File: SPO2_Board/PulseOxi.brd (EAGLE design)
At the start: 70 x 70 mm, 45 parts, among them IC1 AFE4400RHAR

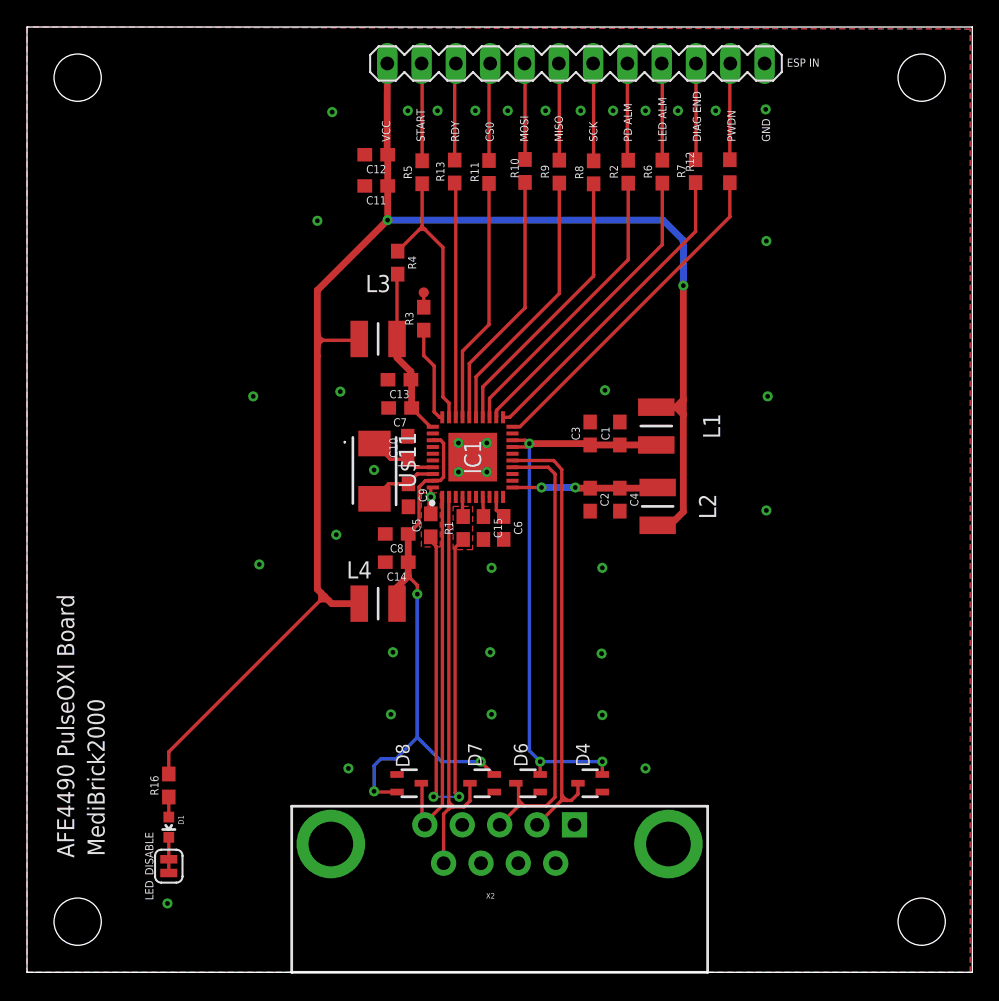
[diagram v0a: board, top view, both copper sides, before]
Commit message: Board Updates
All LEDs at same location
Separated analog and digital ground
Updated impedance components
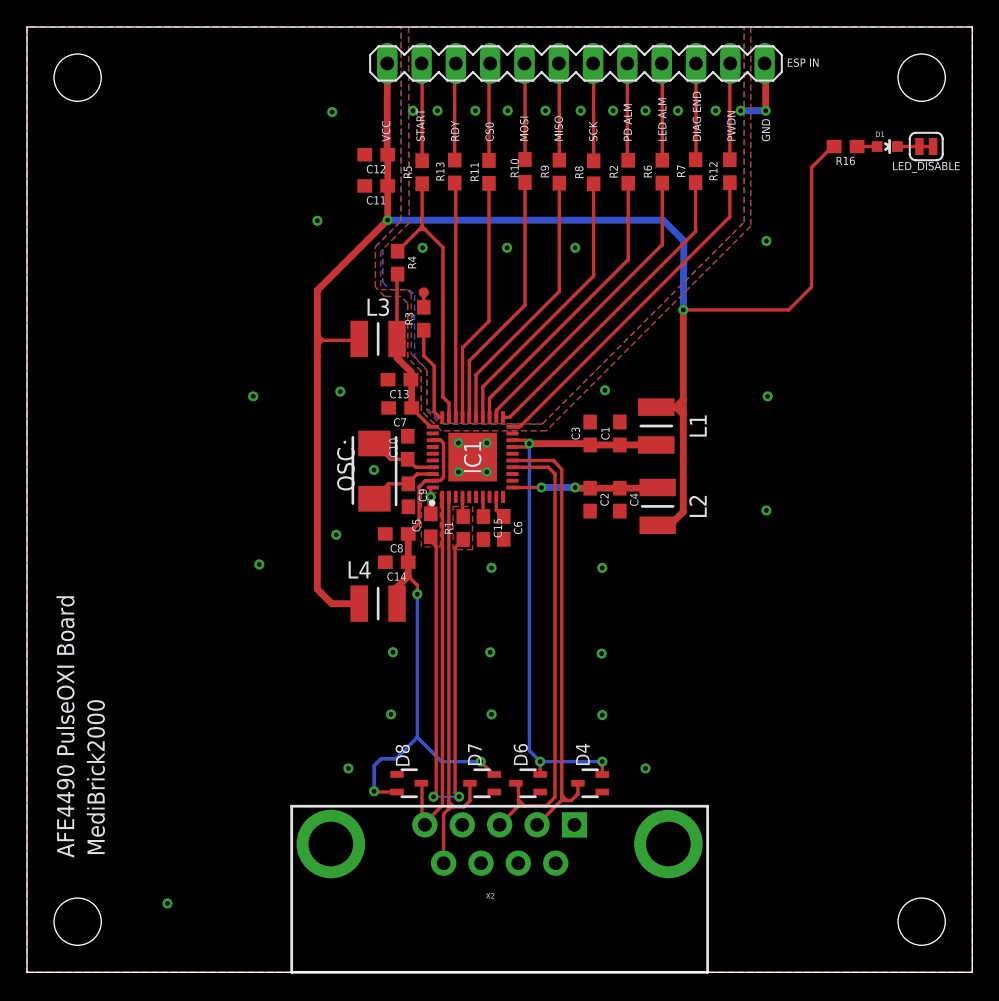
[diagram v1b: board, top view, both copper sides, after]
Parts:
- moved LED_DISABLE 77.4 mm to (66.6, 61.1), turned to 180 degrees
- moved D1 73.3 mm to (63.7, 61.1), turned to 270 degrees
- moved R16 68.9 mm to (60.6, 61.1), turned to 180 degrees
- renumbered U$11 to OSC
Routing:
- net GND: track 7.73 -> 13.1 mm, vias 38 -> 42
- net VCC: track 116.1 -> 118.4 mm

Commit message: Board Updates
Separated analog and digital ground
Updated routing
Updated silk labeling
Sound board with ES8388 included
Impedance and ECG board
Working on IMU board
Working on Environmental Airquality board
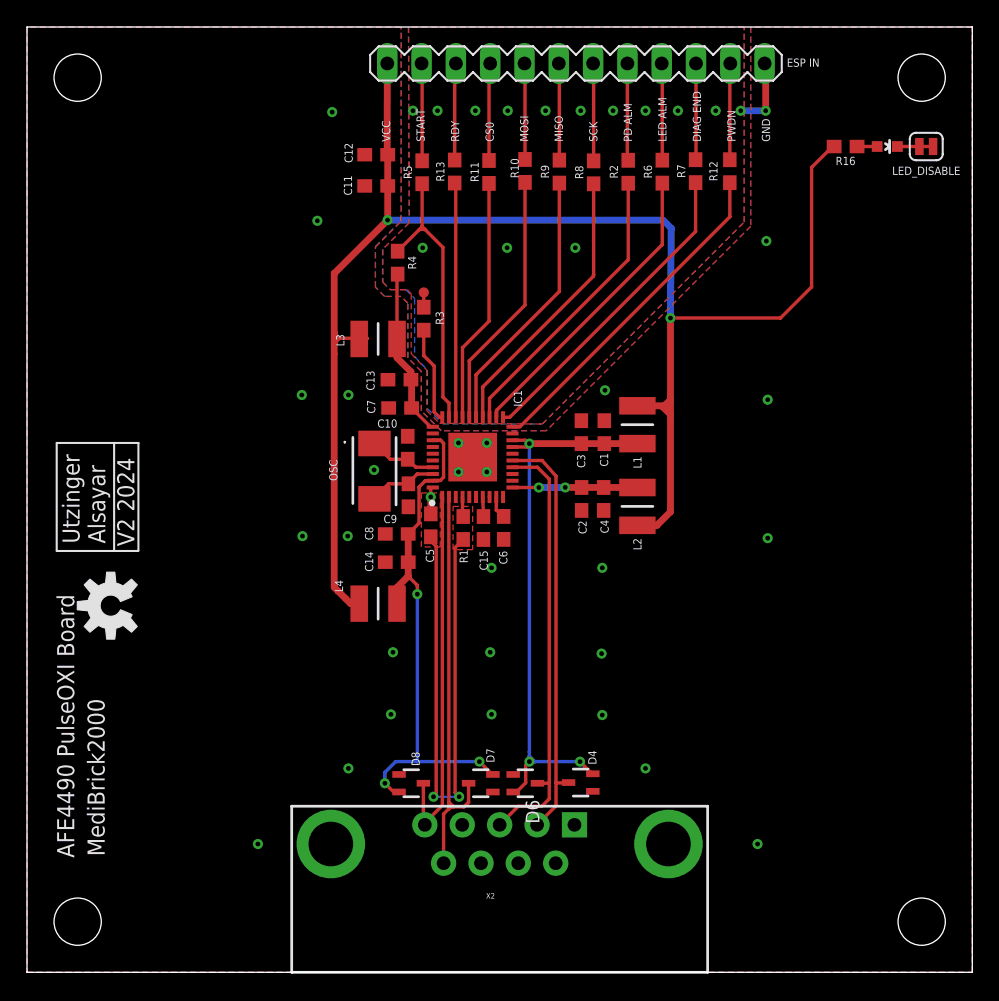
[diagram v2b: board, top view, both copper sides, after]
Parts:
- added U$1: (no value), SparkFun-Aesthetics:OSHW-LOGO-M
- moved L2 1.50 mm to (45.2, 34.5)
- moved L1 1.40 mm to (45.2, 40.5)
- moved C4 1.20 mm to (42.7, 35.1)
- moved C1 1.15 mm to (42.8, 40.0)
- moved D4 0.70 mm to (41.0, 14.1)
- moved C3 0.66 mm to (41.0, 40.0)
- moved C2 0.63 mm to (41.1, 35.1)
- moved D6 0.20 mm to (36.9, 14.0), turned to 270 degrees
- moved D8 0.15 mm to (28.4, 14.0)
- moved D7 0.10 mm to (33.6, 14.0)
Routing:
- net TXP: track 33.7 -> 31.1 mm
- net TXN: track 34.6 -> 32.1 mm
- net RX_ANA_SUP: track 41.6 -> 39.7 mm
- net TX_CTRL_SUP: track 10.8 -> 9.25 mm
- net LED_DRV_SUP: track 42.5 -> 43.1 mm
- net GND: vias 42 -> 43
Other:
- board text added: "Utzinger Alsayar"
- board text added: "V2 2024"

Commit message: IMU board
Completed IMU board design
Updated designs with ground via close to any other via.
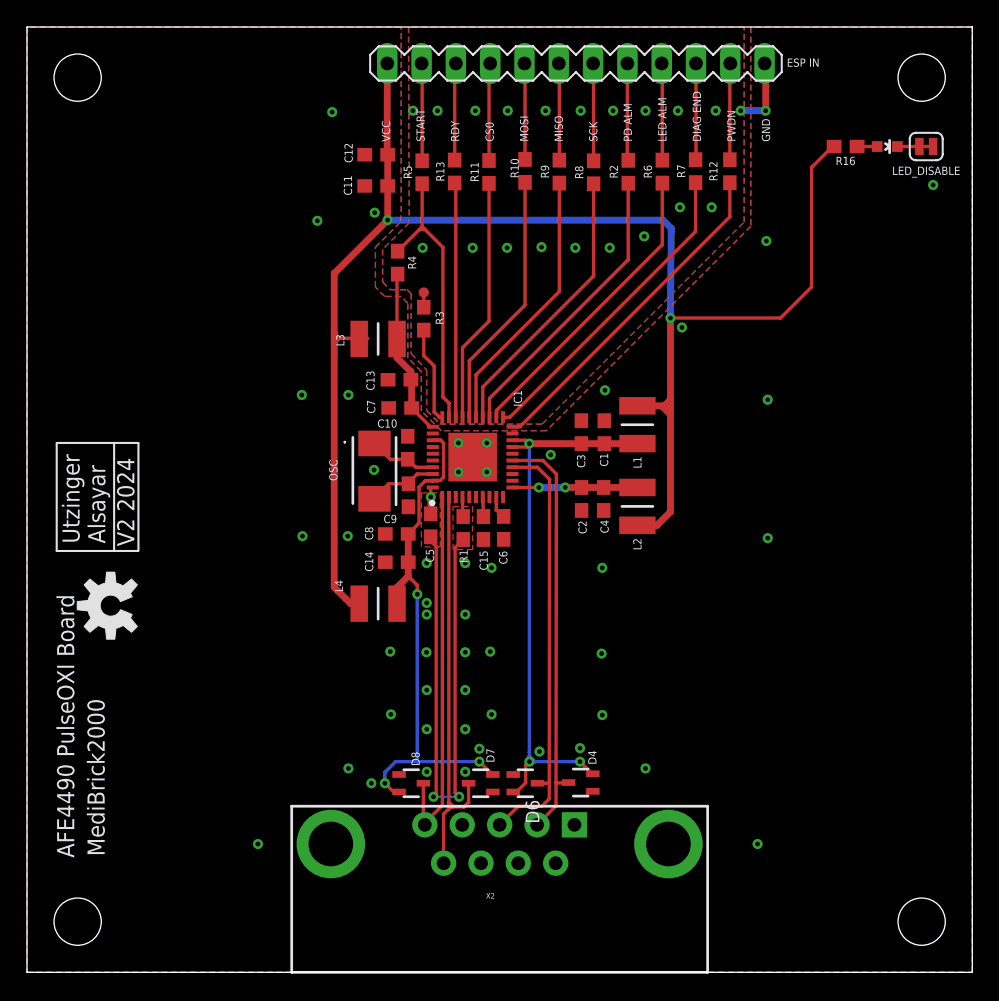
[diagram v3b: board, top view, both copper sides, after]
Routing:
- net GND: vias 43 -> 70
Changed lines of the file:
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@@
 <drawing>
 <settings>
-<setting alwaysvectorfont="no"/>
+<setting alwaysvectorfont="yes"/>
 <setting verticaltext="up"/>
 </settings>
@@
 <contactref element="C1" pad="2"/>
 <contactref element="C2" pad="2"/>
-<polygon width="0.1524" layer="1">
+<polygon width="0.0762" layer="1">
 <vertex x="0" y="70"/>
 <vertex x="0" y="0"/>
@@
 <via x="23.8" y="15.1" extent="1-16" drill="0.35"/>
 <via x="26.95" y="19.1" extent="1-16" drill="0.35"/>
-<via x="27.1" y="23.7" extent="1-16" drill="0.35"/>
+<via x="26.9" y="23.75" extent="1-16" drill="0.35"/>
 <via x="17.1" y="9.5" extent="1-16" drill="0.35"/>
 <contactref element="C5" pad="2"/>
@@
 <wire x1="33" y1="38.1" x2="34.05" y2="37.05" width="0.1524" layer="1"/>
 <via x="34.4" y="19.1" extent="1-16" drill="0.35"/>
-<via x="34.3" y="23.7" extent="1-16" drill="0.35"/>
+<via x="34.3" y="23.75" extent="1-16" drill="0.35"/>
 <via x="34.4" y="29.95" extent="1-16" drill="0.35"/>
 <via x="20.4" y="32.3" extent="1-16" drill="0.35"/>
@@
 <vertex x="29.6" y="44.6"/>
 <vertex x="29.6" y="41.6"/>
-<vertex x="30.546" y="40.654"/>
+<vertex x="30.546" y="40.6"/>
 <vertex x="38.15" y="40.6"/>
 <vertex x="53.1" y="55.55"/>
@@
 <vertex x="28.25" y="70"/>
 <vertex x="28.303796875" y="55.503796875"/>
-<vertex x="26.35" y="53.55"/>
-<vertex x="26.35" y="51.1"/>
+<vertex x="26.334" y="53.534"/>
+<vertex x="26.334" y="51.116"/>
 <vertex x="26.9" y="50.55"/>
-<vertex x="28.046" y="50.55"/>
-<vertex x="28.7" y="49.896"/>
-<vertex x="28.7" y="45.60225"/>
-<vertex x="29.65" y="44.6"/>
-<vertex x="29.65" y="41.75"/>
-<vertex x="30.8" y="40.6"/>
+<vertex x="28.146" y="50.55"/>
+<vertex x="28.45" y="50.246"/>
+<vertex x="28.45" y="45.81325"/>
+<vertex x="29.6" y="44.6"/>
+<vertex x="29.6" y="41.6"/>
+<vertex x="30.6" y="40.6"/>
 <vertex x="38.15" y="40.6"/>
 <vertex x="53.1" y="55.55"/>
@@
 <vertex x="26.5" y="50.05"/>
 <vertex x="25.8" y="50.75"/>
-<vertex x="25.8" y="53.75"/>
-<vertex x="27.7" y="55.65"/>
+<vertex x="25.8" y="53.7"/>
+<vertex x="27.7" y="55.6"/>
 <vertex x="27.7" y="70"/>
 </polygon>
@@
 <wire x1="54.7" y1="67.22" x2="54.62" y2="67.3" width="0.508" layer="1"/>
 <via x="54.1" y="9.5" extent="1-16" drill="0.35"/>
+<via x="32.45" y="30.3" extent="1-16" drill="0.35"/>
+<via x="32.45" y="26.5" extent="1-16" drill="0.35"/>
+<via x="32.45" y="23.7" extent="1-16" drill="0.35"/>
+<via x="32.45" y="20.9" extent="1-16" drill="0.35"/>
+<via x="32.45" y="18" extent="1-16" drill="0.35"/>
+<via x="29.6" y="18" extent="1-16" drill="0.35"/>
+<via x="29.6" y="20.9" extent="1-16" drill="0.35"/>
+<via x="29.577" y="23.7" extent="1-16" drill="0.35"/>
+<via x="29.6" y="26.5" extent="1-16" drill="0.35"/>
+<via x="29.6" y="30.3" extent="1-16" drill="0.35"/>
+<via x="29.6" y="14.85" extent="1-16" drill="0.35"/>
+<via x="32.45" y="14.85" extent="1-16" drill="0.35"/>
+<via x="33" y="53.65" extent="1-16" drill="0.35"/>
+<via x="38.1" y="53.7" extent="1-16" drill="0.35"/>
+<via x="43.15" y="53.65" extent="1-16" drill="0.35"/>
+<via x="45.7" y="54.5" extent="1-16" drill="0.35"/>
+<via x="48.35" y="56.65" extent="1-16" drill="0.35"/>
+<via x="50.7" y="56.65" extent="1-16" drill="0.35"/>
+<via x="67.1" y="58.3" extent="1-16" drill="0.35"/>
+<via x="25.5" y="14" extent="1-16" drill="0.35"/>
+<via x="33.5" y="16.55" extent="1-16" drill="0.35"/>
+<via x="37.95" y="16.35" extent="1-16" drill="0.35"/>
+<via x="40.95" y="16.6" extent="1-16" drill="0.35"/>
+<via x="29.6" y="27.35" extent="1-16" drill="0.35"/>
+<via x="38.781" y="38.319" extent="1-16" drill="0.35"/>
+<via x="48.5" y="47.75" extent="1-16" drill="0.35"/>
+<via x="25.75" y="56.25" extent="1-16" drill="0.35"/>
 </signal>
 <signal name="PWDN">
@@
 <contactref element="X2" pad="3"/>
 <contactref element="D6" pad="1"/>
-<wire x1="38.673" y1="36.527" x2="38.673" y2="14" width="0.254" layer="1"/>
+<wire x1="38.7" y1="36.5" x2="38.673" y2="14" width="0.254" layer="1"/>
 <contactref element="IC1" pad="14"/>
 <wire x1="38.673" y1="14" x2="38.673" y2="12.843" width="0.254" layer="1"/>
 <wire x1="35.95" y1="37.4" x2="37.8" y2="37.4" width="0.254" layer="1"/>
-<wire x1="37.8" y1="37.4" x2="38.673" y2="36.527" width="0.254" layer="1"/>
+<wire x1="37.8" y1="37.4" x2="38.7" y2="36.5" width="0.254" layer="1"/>
 <wire x1="38.1192" y1="12.2892" x2="36.3692" y2="12.2892" width="0.254" layer="1"/>
 <wire x1="38.673" y1="12.843" x2="38.1192" y2="12.2892" width="0.254" layer="1"/>
@@
 <contactref element="X2" pad="2"/>
 <contactref element="D4" pad="1"/>
-<wire x1="38.1451625" y1="37.9" x2="39.173" y2="36.74134375" width="0.254" layer="1"/>
+<wire x1="38.2" y1="37.9" x2="39.2" y2="36.9" width="0.254" layer="1"/>
 <contactref element="IC1" pad="15"/>
-<wire x1="35.95" y1="37.9" x2="38.1451625" y2="37.9" width="0.254" layer="1"/>
+<wire x1="35.95" y1="37.9" x2="38.2" y2="37.9" width="0.254" layer="1"/>
 <wire x1="40.1" y1="14.05" x2="40.1" y2="14.025" width="0.254" layer="1"/>
 <wire x1="37.77" y1="10.92" x2="39.175" y2="12.325" width="0.254" layer="1"/>
 <wire x1="40.1" y1="14.025" x2="39.173" y2="14.025" width="0.254" layer="1"/>
 <wire x1="39.173" y1="12.327" x2="39.175" y2="12.325" width="0.254" layer="1"/>
-<wire x1="39.173" y1="36.74134375" x2="39.173" y2="14.025" width="0.254" layer="1"/>
+<wire x1="39.2" y1="36.9" x2="39.173" y2="14.025" width="0.254" layer="1"/>
 <wire x1="39.175" y1="12.325" x2="39.175" y2="14.023" width="0.254" layer="1"/>
 <wire x1="39.175" y1="14.023" x2="39.173" y2="14.025" width="0.254" layer="1"/>

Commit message: Production Updates
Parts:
- moved R4 8.59 mm to (28.7, 44.0), turned to 180 degrees
- moved TP2 8.32 mm to (26.8, 42.4)
- moved R3 5.99 mm to (28.7, 42.5), turned to 180 degrees
- moved C7 3.29 mm to (25.2, 44.0)
- moved C13 2.87 mm to (25.2, 45.5)
- moved R8 2.01 mm to (41.9, 61.2)
- moved R5 2.00 mm to (29.2, 61.2)
- moved R11 1.98 mm to (34.2, 61.2)
- moved R2 1.96 mm to (44.5, 61.2)
- moved R6 1.96 mm to (47.0, 61.2)
- moved R9 1.95 mm to (39.4, 61.2)
- moved R13 1.95 mm to (31.7, 61.2)
- moved R12 1.92 mm to (52.0, 61.2)
- moved R7 1.92 mm to (49.5, 61.2)
- moved R10 1.90 mm to (36.8, 61.2)
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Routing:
- net VCC: track 118.4 -> 107.5 mm
- net N$2: track 7.13 -> 2.16 mm
- net RX_ANA_SUP: track 39.7 -> 42.3 mm
- net SCK: track 7.23 -> 5.21 mm
- net RESET: track 7.22 -> 5.21 mm
- net N$12: track 20.7 -> 22.7 mm
- net LEDALARM: track 7.18 -> 5.21 mm
- net MISO: track 7.18 -> 5.21 mm
- net CS: track 7.22 -> 5.26 mm
- net N$15: track 18.1 -> 20.1 mm
- net N$8: track 17.4 -> 19.3 mm
- net ADCRDY: track 7.19 -> 5.24 mm
- net PD_ALM_OUT: track 7.20 -> 5.25 mm
- net N$11: track 21.6 -> 23.5 mm
- net N$10: track 22.4 -> 24.4 mm
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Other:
- board text added: "AFE4490 PulseOx Board"
- board text added: "DIAG_E"
- board text added: "MediBrick 2000"
- board text added: "V3 2024"
- board text removed: "AFE4490 PulseOXI Board"
- board text removed: "DIAG END"
- board text removed: "ESP IN"
- board text removed: "MediBrick2000"
- board text removed: "V2 2024"

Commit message: Merging Production Status to Github, Obtaining senior design files
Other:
- board text added: "LED_A"
- board text added: "PD_A"
- board text removed: "LED ALM"
- board text removed: "PD ALM"
